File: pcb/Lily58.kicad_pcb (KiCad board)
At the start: 2 copper layers, 142.5 x 106.3 mm, 132 parts, among them J2 4PIN, J3 Conn_01x06_Female, J4 Conn_01x06_Female, P1 i2c_pin, P2 i2c_pin, SW1 SW_PUSH, SW10 SW_PUSH, SW11 SW_PUSH, SW12 SW_PUSH, SW13 SW_PUSH, SW14 SW_PUSH, SW15 SW_PUSH, SW16 SW_PUSH, SW17 SW_PUSH, SW18 SW_PUSH, SW19 SW_PUSH, SW2 SW_PUSH, SW20 SW_PUSH, SW21 SW_PUSH, SW22 SW_PUSH, SW23 SW_PUSH, SW24 SW_PUSH, SW25 SW_PUSH, SW26 SW_PUSH, SW27 SW_PUSH, SW28 SW_PUSH, SW29 SW_PUSH, SW3 SW_PUSH, SW4 SW_PUSH, SW5 SW_PUSH, SW6 SW_PUSH, SW7 SW_PUSH, SW8 SW_PUSH, SW9 SW_PUSH, U1 ProMicro

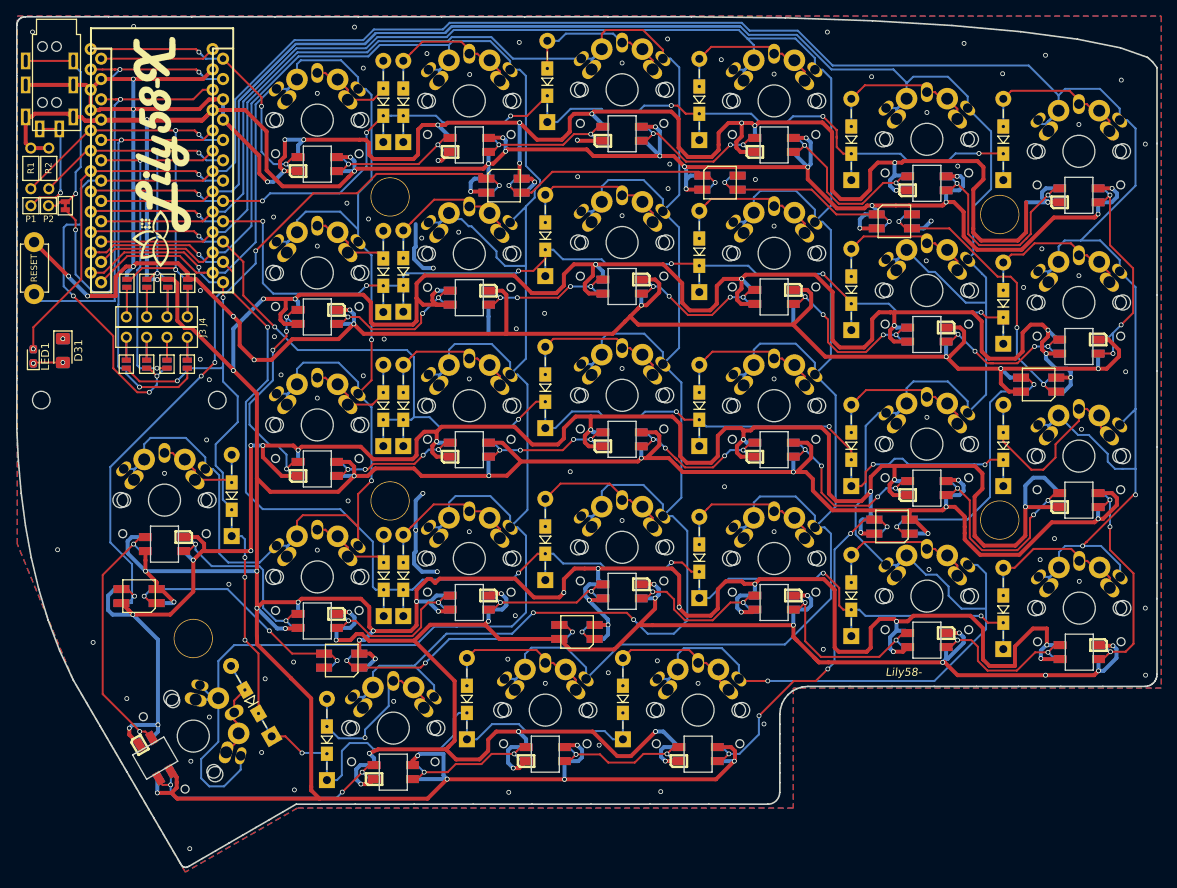
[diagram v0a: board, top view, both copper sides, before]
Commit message: update sk6812mini pin assgin
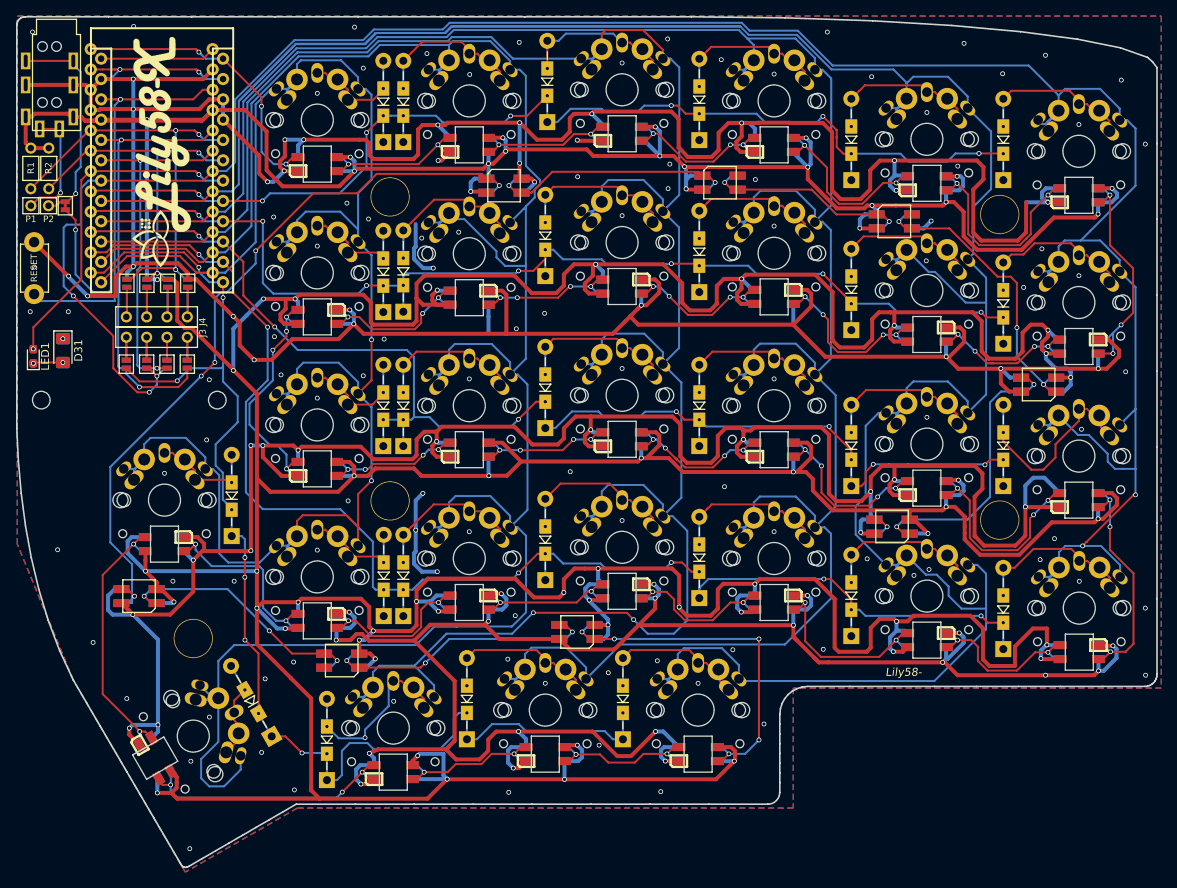
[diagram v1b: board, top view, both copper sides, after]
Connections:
- L31 pad 1: Net-(L31-Pad1) -> Net-(L30-Pad3)
- L31 pad 3: Net-(L30-Pad1) -> Net-(L31-Pad3)
- L32 pad 1: Net-(L32-Pad1) -> Net-(L31-Pad3)
- L32 pad 3: Net-(L31-Pad1) -> Net-(L32-Pad3)
- L33 pad 1: Net-(L33-Pad1) -> Net-(L32-Pad3)
- L33 pad 3: Net-(L32-Pad1) -> Net-(L33-Pad3)
- L34 pad 1: Net-(L34-Pad1) -> Net-(L33-Pad3)
- L34 pad 3: Net-(L33-Pad1) -> Net-(L34-Pad3)
- L35 pad 1: Net-(L35-Pad1) -> Net-(L34-Pad3)
- L35 pad 3: Net-(L34-Pad1) -> Net-(L29-Pad1)
- L36 pad 1: Net-(L30-Pad3) -> Net-(L36-Pad1)
- L36 pad 3: Net-(L36-Pad3) -> Net-(L30-Pad1)
- L37 pad 1: Net-(L36-Pad3) -> Net-(L37-Pad1)
- L37 pad 3: Net-(L29-Pad1) -> Net-(L36-Pad1)
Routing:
- net Net-(L32-Pad3): track 0.00 -> 92.2 mm, vias 0 -> 5
- net Net-(L32-Pad1): track 92.2 -> 0.00 mm, vias 5 -> 0
- net Net-(L36-Pad3): track 33.8 -> 0.00 mm, vias 2 -> 0
- net Net-(L36-Pad1): track 0.00 -> 33.8 mm, vias 0 -> 2
- net Net-(L34-Pad3): track 0.00 -> 31.4 mm, vias 0 -> 3
- net Net-(L34-Pad1): track 31.4 -> 0.00 mm, vias 3 -> 0
- net Net-(L31-Pad3): track 0.00 -> 30.2 mm, vias 0 -> 2
- net Net-(L31-Pad1): track 30.2 -> 0.00 mm, vias 2 -> 0
- net Net-(L33-Pad3): track 0.00 -> 29.2 mm, vias 0 -> 3
- net Net-(L33-Pad1): track 29.2 -> 0.00 mm, vias 3 -> 0
- net Net-(L30-Pad3): track 38.0 -> 26.5 mm, vias 3 -> 2
- net Net-(L30-Pad1): track 26.5 -> 38.0 mm, vias 2 -> 3
- net Net-(L35-Pad1): track 2.47 -> 0.00 mm, vias 1 -> 0
- net Net-(L37-Pad1): track 0.00 -> 2.46 mm, vias 0 -> 1
- net Net-(L29-Pad1): track 46.0 -> 43.7 mm
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
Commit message: change pcb - delete underglow - change pins - change holes for sk6812mini-e
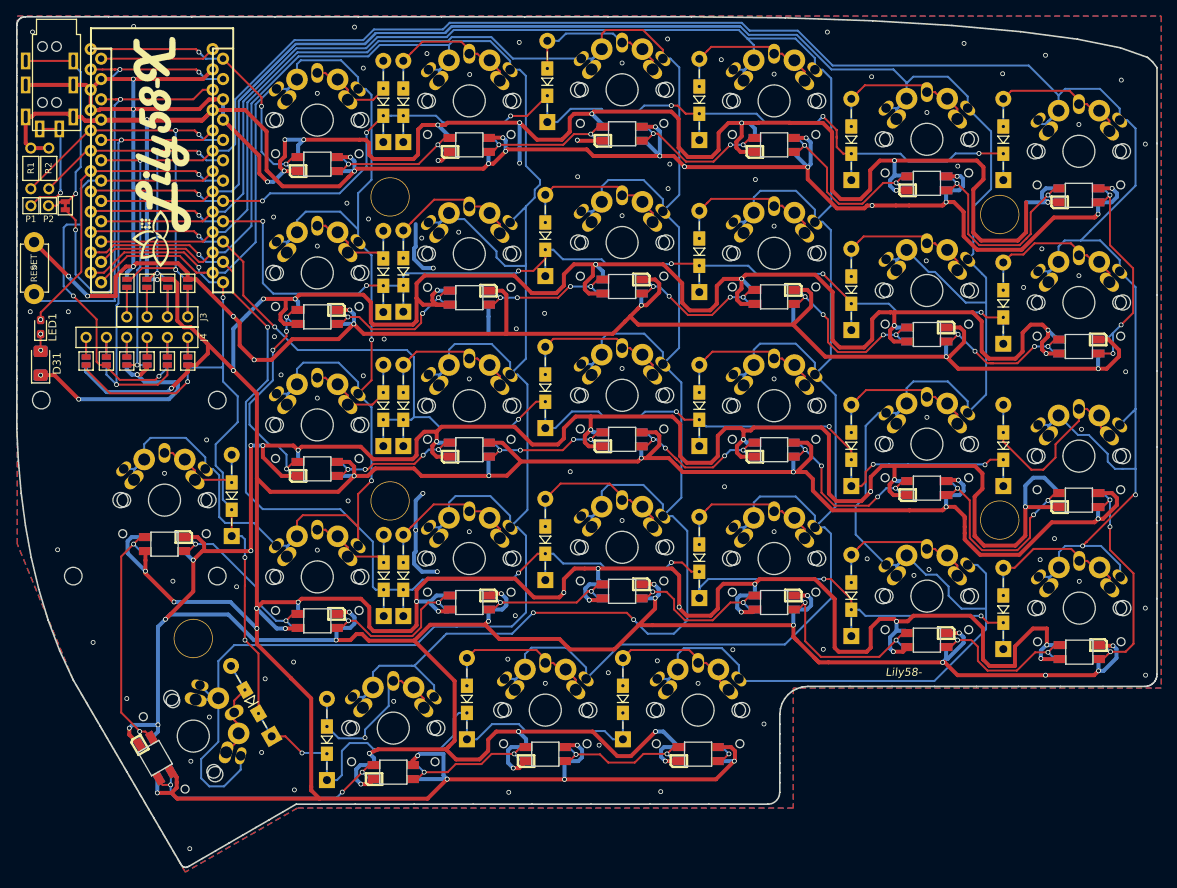
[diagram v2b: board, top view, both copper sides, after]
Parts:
- removed L30, L31, L32, L33, L34, L35, L36, L37: SK6812mini, Lily58-footprint:SK6812MINI_underglow_rev
- added JP17: Jumper_NO_Small, Lily58-footprint:Jumper, B.Cu at (101.8, 80.1)
- added JP18: Jumper_NO_Small, Lily58-footprint:Jumper, B.Cu at (104.3, 80.1)
- added JP19: Jumper_NO_Small, Lily58-footprint:Jumper, F.Cu at (101.8, 80.1)
- added JP20: Jumper_NO_Small, Lily58-footprint:Jumper, F.Cu at (104.3, 80.1)
- added TH8: HOLE, Lily58-footprint:HOLE_M2, F.Cu at (108.0, 107.0)
- added TH9: HOLE, Lily58-footprint:HOLE_M2, F.Cu at (90.0, 107.0)
- J4: footprint Lily58-footprint:OLED_4Pin -> Lily58-footprint:OLED_6Pin
- moved JP13 12.7 mm to (91.6, 80.1)
- moved JP9 12.7 mm to (91.6, 80.1)
- moved J4 12.6 mm to (91.6, 77.2), turned to 0 degrees
- moved JP10 7.58 mm to (94.1, 80.1)
- moved JP14 7.58 mm to (94.1, 80.1)
- moved LED1 3.77 mm to (85.9, 75.9)
- moved D31 3.20 mm to (85.9, 80.4), turned to 90 degrees
- moved JP12 2.62 mm to (99.2, 80.1)
- moved JP16 2.62 mm to (99.2, 80.1)
- moved JP11 2.52 mm to (96.7, 80.1)
- moved JP15 2.52 mm to (96.7, 80.1)
- moved J3 0.05 mm to (104.3, 74.6)
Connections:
- JP10 pad 2: col0 -> A3
- JP11 pad 2: A2 -> GND
- JP12 pad 2: A3 -> col0
- JP13 pad 2: A3 -> row4
- JP16 pad 2: row4 -> GND
- JP9 pad 2: row4 -> VCC
- U1 pad 18: col0 -> A2
- U1 pad 19: A2 -> col0
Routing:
- net Net-(L32-Pad3): track 92.2 -> 0.00 mm, vias 5 -> 0
- net VCC: track 1082.9 -> 1042.5 mm, vias 66 -> 58
- net Net-(L29-Pad1): track 43.7 -> 3.64 mm, vias 5 -> 1
- net Net-(L30-Pad1): track 38.0 -> 0.00 mm, vias 3 -> 0
- net Net-(L36-Pad1): track 33.8 -> 0.00 mm, vias 2 -> 0
- net Net-(L34-Pad3): track 31.4 -> 0.00 mm, vias 3 -> 0
- net Net-(L31-Pad3): track 30.2 -> 0.00 mm, vias 2 -> 0
- net Net-(L33-Pad3): track 29.2 -> 0.00 mm, vias 3 -> 0
- net Net-(L30-Pad3): track 26.5 -> 0.00 mm, vias 2 -> 0
- net col0: track 312.5 -> 297.0 mm, vias 5 -> 4
- net GND: track 1051.5 -> 1062.9 mm, vias 165 -> 162
- net A2: track 44.1 -> 53.5 mm
- net row4: track 158.7 -> 166.8 mm, vias 7 -> 6
- net Net-(J4-Pad6): track 0.00 -> 4.90 mm
- net Net-(J4-Pad5): track 0.00 -> 4.90 mm
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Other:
- outline, holes or cut-outs redrawn

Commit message: update pcb
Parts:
- moved J3 1.00 mm to (104.3, 73.6)
- moved J4 0.27 mm to (91.6, 77.4)
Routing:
- net GND: track 1062.9 -> 1089.5 mm, vias 162 -> 163
- net Net-(J3-Pad3): track 8.23 -> 5.40 mm
- net Net-(J3-Pad2): track 8.22 -> 5.40 mm
- net Net-(J3-Pad1): track 8.22 -> 5.40 mm
- net Net-(J3-Pad4): track 8.20 -> 5.40 mm
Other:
- board text added: "Lot.001"

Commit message: update pcb
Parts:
- removed D31: S-562T, Lily58-footprint:D_1206_3216Metric_Pad1.42x1.75mm_HandSolder
- removed LED1: SMLE13BC8TT86, Lily58-footprint:LED_0603_1608Metric_Pad1.05x0.95mm_HandSolder
- removed P1, P2: i2c_pin, Lily58-footprint:1pin_conn
- removed W1: jumper, Lily58-footprint:jumper_data
- added D/R: S-562T, Lily58-footprint:D_1206_3216Metric_Pad1.42x1.75mm_HandSolder, F.Cu at (86.9, 76.9)
- added JP21: 1S, Lily58-footprint:Jumper, F.Cu at (84.7, 61.5)
- added JP22: I2C, Lily58-footprint:Jumper, F.Cu at (86.9, 61.5)
- added LED: SMLE13BC8TT86, Lily58-footprint:LED_0603_1608Metric_Pad1.05x0.95mm_HandSolder, F.Cu at (84.7, 76.9)
- moved RSW1 1.04 mm to (84.7, 69.5)
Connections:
- J2 pad 1: VCC -> Net-(J2-Pad1)
- J2 pad 2: GND -> SDA
- J2 pad 3: Net-(J2-Pad3) -> GND
- J2 pad 4: Net-(J2-Pad4) -> VCC
- JP20 pad 2: VCC -> DATA
- JP9 pad 2: VCC -> DATA
- U1 pad 7: Net-(LED1-Pad2) -> D4
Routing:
- net D4: track 0.00 -> 39.8 mm, vias 0 -> 3
- net Net-(LED1-Pad2): track 38.2 -> 0.00 mm, vias 2 -> 0
- net DATA: track 59.1 -> 90.3 mm, vias 3 -> 6
- net Net-(J2-Pad3): track 26.7 -> 0.00 mm, vias 1 -> 0
- net Net-(J2-Pad1): track 0.00 -> 25.0 mm, vias 0 -> 1
- net Net-(J2-Pad4): track 14.8 -> 0.00 mm, vias 1 -> 0
- net SDA: track 53.7 -> 66.5 mm
- net VCC: track 1042.5 -> 1033.9 mm, vias 58 -> 61
- net A2: track 53.5 -> 49.1 mm
- net GND: track 1089.5 -> 1092.8 mm, vias 163 -> 158
- net SCL: track 42.8 -> 45.2 mm
- net RESET: track 50.5 -> 52.5 mm
- net Net-(D31-Pad2): track 2.17 -> 3.28 mm
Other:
- board text removed: "LED1"

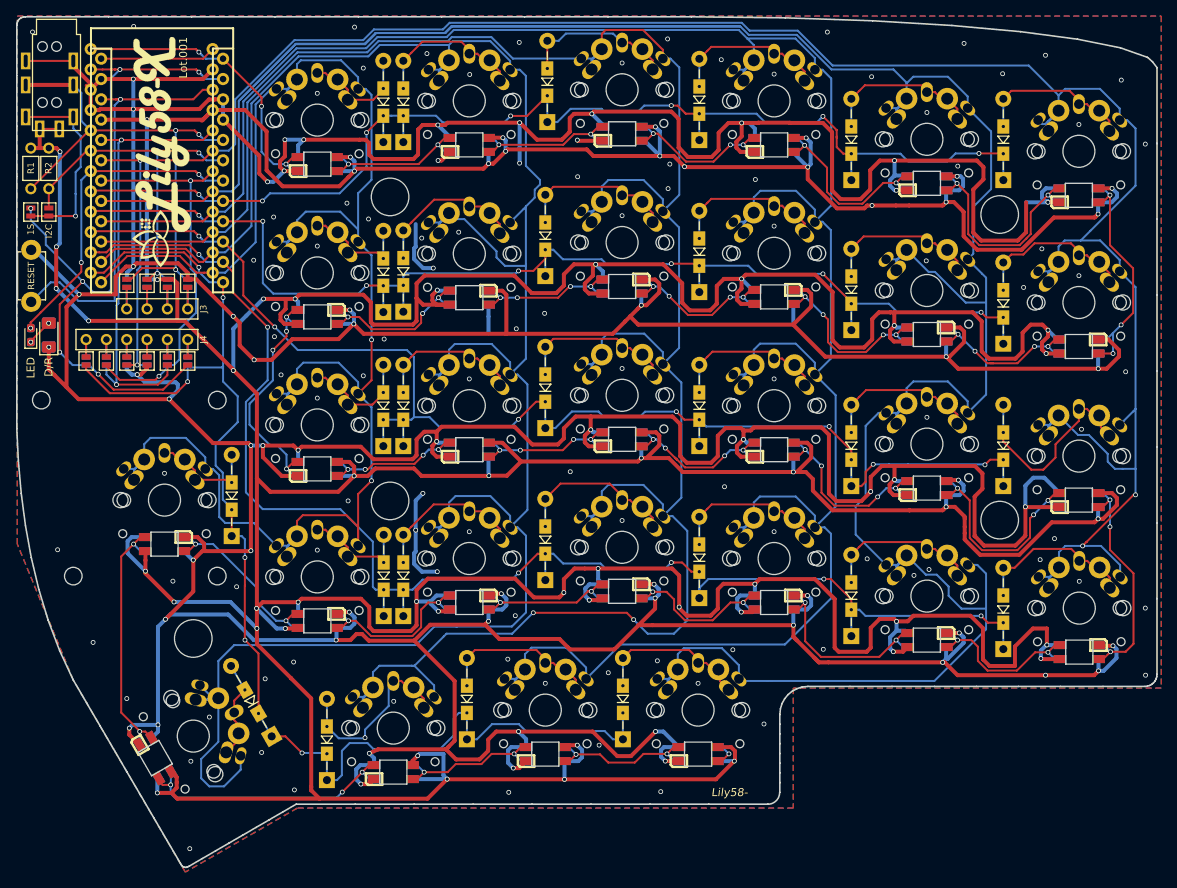
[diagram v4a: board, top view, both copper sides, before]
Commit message: add underglow
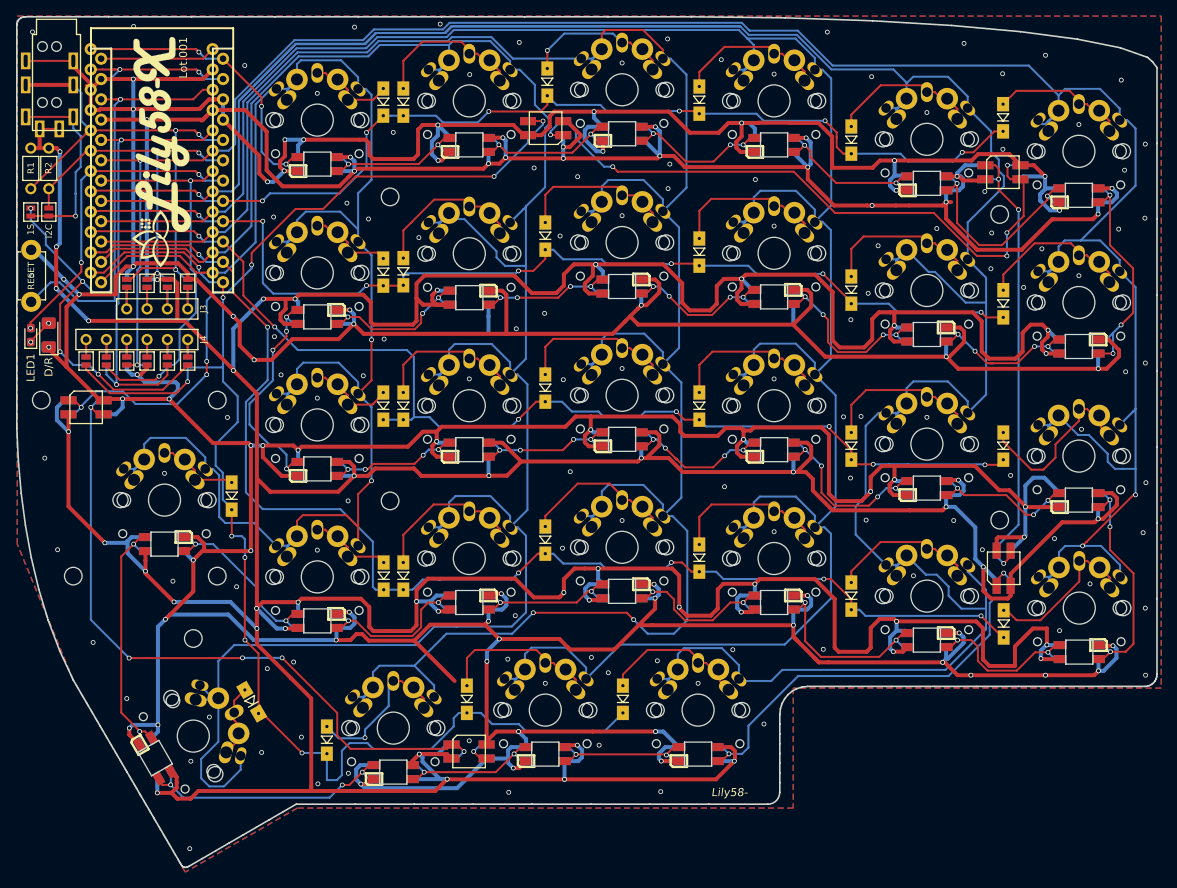
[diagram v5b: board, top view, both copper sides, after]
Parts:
- added D32: SK6812MINI, Lily58-footprint:SK6812MINI_underglow_rev, F.Cu at (139.5, 128.9)
- added D33: SK6812MINI, Lily58-footprint:SK6812MINI_underglow_rev, F.Cu at (91.6, 85.9)
- added D34: SK6812MINI, Lily58-footprint:SK6812MINI_underglow_rev, F.Cu at (149.0, 51.0)
- added D35: SK6812MINI, Lily58-footprint:SK6812MINI_underglow_rev, F.Cu at (206.2, 56.5)
- added D36: SK6812MINI, Lily58-footprint:SK6812MINI_underglow_rev, F.Cu at (206.3, 106.0)
- D1, D10, D11, D12, D13, D14, D15, D16, D17, D18, D19, D2, D20, D21, D22, D23, D24, D25, D26, D27, D28, D29, D3, D4, D5, D6, D7, D8, D9: footprint Lily58-footprint:Diode_TH_SOD123 -> Lily58-footprint:Diode_SOD123
- TH3, TH4, TH5, TH6, TH7: footprint Lily58-footprint:HOLE_M2_TH -> Lily58-footprint:HOLE_M2
- moved D6 2.79 mm to (206.2, 49.7)
- moved D24 1.85 mm to (206.3, 113.0)
- renumbered LED to LED1
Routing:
- net Net-(D32-Pad3): track 0.00 -> 88.1 mm, vias 0 -> 5
- net Net-(D33-Pad3): track 0.00 -> 87.1 mm, vias 0 -> 6
- net Net-(D34-Pad3): track 0.00 -> 82.5 mm, vias 0 -> 5
- net VCC: track 1033.9 -> 1094.6 mm, vias 61 -> 65
- net Net-(D35-Pad3): track 0.00 -> 57.4 mm, vias 0 -> 3
- net Net-(D36-Pad3): track 3.64 -> 55.4 mm, vias 1 -> 2
- net GND: track 1092.8 -> 1048.5 mm, vias 158 -> 182
- net row2: track 163.0 -> 141.2 mm
- net row3: track 181.1 -> 160.6 mm
- net row1: track 150.1 -> 130.3 mm
- net row0: track 149.6 -> 130.1 mm
- net Net-(L17-Pad1): track 26.5 -> 18.7 mm
- net row4: track 166.8 -> 159.4 mm, vias 6 -> 7
- net Net-(D32-Pad1): track 0.00 -> 3.92 mm, vias 0 -> 1
- net Net-(L4-Pad1): track 23.0 -> 19.5 mm
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
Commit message: update PCB
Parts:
- renumbered D/R to D31
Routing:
- net VCC: track 1094.6 -> 1064.1 mm, vias 65 -> 64
- net GND: track 1048.5 -> 1028.8 mm, vias 182 -> 181
- net Net-(L22-Pad3): track 22.8 -> 18.3 mm
- net Net-(L16-Pad1): track 22.7 -> 18.9 mm
- net Net-(L19-Pad3): track 20.6 -> 17.7 mm
- net col3: track 288.8 -> 285.9 mm, vias 2 -> 0
- net Net-(L21-Pad3): track 19.6 -> 17.0 mm
- net Net-(L15-Pad1): track 18.9 -> 16.4 mm
- net Net-(L23-Pad3): track 20.9 -> 18.5 mm
- net Net-(L11-Pad3): track 19.3 -> 17.2 mm
- net Net-(L3-Pad1): track 18.9 -> 17.2 mm
